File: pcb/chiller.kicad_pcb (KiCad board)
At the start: 2 copper layers, 94 x 57 mm, 68 parts, among them J1 Temp sensor 1, J10 Fan, J11 Display, J12 Debug, J13 Conn_01x04, J14 Flow sensor, J15 Buzzer, J2 Temp sensor 2, J3 Ext, J4 Mains in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

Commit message: Fix footprint.
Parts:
- D8: footprint Diode_SMD:D_SMC -> Diode_SMD:D_SMA
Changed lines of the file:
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@@
     )
   )
-  (footprint "Diode_SMD:D_SMC" (layer "F.Cu")
+  (footprint "Diode_SMD:D_SMA" (layer "F.Cu")
     (at 101.4984 128.524)
-    (descr "Diode SMC (DO-214AB)")
-    (tags "Diode SMC (DO-214AB)")
-    (property "Reference" "D8" (at -1.6764 -4.9784 0) (layer "F.SilkS") hide
+    (descr "Diode SMA (DO-214AC)")
+    (tags "Diode SMA (DO-214AC)")
+    (property "Reference" "D8" (at 0 -2.5 0) (layer "F.SilkS")
       (effects (font (size 1 1) (thickness 0.15)))
     )
-    (property "Value" "SS34" (at 0 4.2 0) (layer "F.Fab") hide
+    (property "Value" "SS34" (at 0 2.6 0) (layer "F.Fab")
       (effects (font (size 1 1) (thickness 0.15)))
     )
@@
     (sheetfile "chiller.kicad_sch")
     (attr smd)
-    (fp_line (start -4.8 -3.25) (end 3.6 -3.25)
+    (fp_line (start -3.4 -1.65) (end -3.4 1.65)
       (stroke (width 0.12) (type solid)) (layer "F.SilkS"))
-    (fp_line (start -4.8 3.25) (end -4.8 -3.25)
+    (fp_line (start -3.4 -1.65) (end 2 -1.65)
       (stroke (width 0.12) (type solid)) (layer "F.SilkS"))
-    (fp_line (start -4.8 3.25) (end 3.6 3.25)
+    (fp_line (start -3.4 1.65) (end 2 1.65)
       (stroke (width 0.12) (type solid)) (layer "F.SilkS"))
-    (fp_line (start -4.9 -3.35) (end 4.9 -3.35)
+    (fp_line (start -3.5 -1.75) (end 3.5 -1.75)
       (stroke (width 0.05) (type solid)) (layer "F.CrtYd"))
-    (fp_line (start -4.9 3.35) (end -4.9 -3.35)
+    (fp_line (start -3.5 1.75) (end -3.5 -1.75)
       (stroke (width 0.05) (type solid)) (layer "F.CrtYd"))
-    (fp_line (start 4.9 -3.35) (end 4.9 3.35)
+    (fp_line (start 3.5 -1.75) (end 3.5 1.75)
       (stroke (width 0.05) (type solid)) (layer "F.CrtYd"))
-    (fp_line (start 4.9 3.35) (end -4.9 3.35)
+    (fp_line (start 3.5 1.75) (end -3.5 1.75)
       (stroke (width 0.05) (type solid)) (layer "F.CrtYd"))
-    (fp_line (start -3.55 3.1) (end -3.55 -3.1)
+    (fp_line (start -2.3 1.5) (end -2.3 -1.5)
       (stroke (width 0.1) (type solid)) (layer "F.Fab"))
     (fp_line (start -0.64944 -0.79908) (end -0.64944 0.80112)
@@
     (fp_line (start 0.50118 0.75032) (end 0.50118 -0.79908)
       (stroke (width 0.1) (type solid)) (layer "F.Fab"))
-    (fp_line (start 3.55 -3.1) (end -3.55 -3.1)
+    (fp_line (start 2.3 -1.5) (end -2.3 -1.5)
       (stroke (width 0.1) (type solid)) (layer "F.Fab"))
-    (fp_line (start 3.55 -3.1) (end 3.55 3.1)
+    (fp_line (start 2.3 -1.5) (end 2.3 1.5)
       (stroke (width 0.1) (type solid)) (layer "F.Fab"))
-    (fp_line (start 3.55 3.1) (end -3.55 3.1)
+    (fp_line (start 2.3 1.5) (end -2.3 1.5)
       (stroke (width 0.1) (type solid)) (layer "F.Fab"))
-    (fp_text user "${REFERENCE}" (at 0 -1.9 0) (layer "F.Fab")
+    (fp_text user "${REFERENCE}" (at 0 -2.5 0) (layer "F.Fab")
       (effects (font (size 1 1) (thickness 0.15)))
     )
-    (pad "1" smd rect (at -3.4 0 90) (size 3.3 2.5) (layers "F.Cu" "F.Paste" "F.Mask")
+    (pad "1" smd rect (at -2 0) (size 2.5 1.8) (layers "F.Cu" "F.Paste" "F.Mask")
       (net 53 "+12V") (pinfunction "K") (pintype "passive")
     )
-    (pad "2" smd rect (at 3.4 0 90) (size 3.3 2.5) (layers "F.Cu" "F.Paste" "F.Mask")
+    (pad "2" smd rect (at 2 0) (size 2.5 1.8) (layers "F.Cu" "F.Paste" "F.Mask")
       (net 57 "Net-(D8-A)") (pinfunction "A") (pintype "passive")
     )
-    (model "${KICAD6_3DMODEL_DIR}/Diode_SMD.3dshapes/D_SMC.wrl"
+    (model "${KICAD6_3DMODEL_DIR}/Diode_SMD.3dshapes/D_SMA.wrl"
       (offset (xyz 0 0 0))
       (scale (xyz 1 1 1))
@@
   (segment (start 119.6593 125.6029) (end 119.6595 125.6029) (width 0.2) (layer "F.Cu") (net 53))
   (segment (start 120.724374 126.4542) (end 119.949374 125.6792) (width 0.2) (layer "F.Cu") (net 53))
+  (segment (start 99.4984 128.524) (end 104.5276 123.4948) (width 1) (layer "F.Cu") (net 53))
   (segment (start 136.1332 127.9652) (end 132.1044 127.9652) (width 0.2) (layer "F.Cu") (net 53))
-  (segment (start 96.980547 129.9972) (end 91.7448 129.9972) (width 1) (layer "F.Cu") (net 53))
   (segment (start 120.142 121.0964) (end 118.3894 119.3438) (width 0.2) (layer "F.Cu") (net 53))
-  (segment (start 98.0984 128.524) (end 98.0984 128.879347) (width 1) (layer "F.Cu") (net 53))
   (segment (start 90.5456 128.798) (end 90.5456 127.999) (width 1) (layer "F.Cu") (net 53))
+  (segment (start 98.0252 129.9972) (end 99.4984 128.524) (width 1) (layer "F.Cu") (net 53))
   (segment (start 109.8658 119.3184) (end 105.6894 123.4948) (width 1) (layer "F.Cu") (net 53))
   (segment (start 111.2266 119.3184) (end 109.8658 119.3184) (width 1) (layer "F.Cu") (net 53))
   (segment (start 120.142 125.1204) (end 120.142 121.0964) (width 0.2) (layer "F.Cu") (net 53))
-  (segment (start 98.0984 128.879347) (end 96.980547 129.9972) (width 1) (layer "F.Cu") (net 53))
   (segment (start 132.1044 127.9652) (end 131.3688 127.2296) (width 0.2) (layer "F.Cu") (net 53))
   (segment (start 119.583 125.6792) (end 119.688153 125.574047) (width 0.2) (layer "F.Cu") (net 53))
   (segment (start 119.949374 125.6792) (end 119.583 125.6792) (width 0.2) (layer "F.Cu") (net 53))
-  (segment (start 103.1276 123.4948) (end 98.0984 128.524) (width 1) (layer "F.Cu") (net 53))
   (segment (start 131.3688 127.2296) (end 130.684 127.2296) (width 0.2) (layer "F.Cu") (net 53))
   (segment (start 91.7448 129.9972) (end 90.5456 128.798) (width 1) (layer "F.Cu") (net 53))
   (segment (start 121.5266 126.4542) (end 120.724374 126.4542) (width 0.2) (layer "F.Cu") (net 53))
   (segment (start 130.098 126.6436) (end 121.716 126.6436) (width 0.2) (layer "F.Cu") (net 53))
+  (segment (start 104.5276 123.4948) (end 105.6894 123.4948) (width 1) (layer "F.Cu") (net 53))
   (segment (start 111.2266 119.3184) (end 118.364 119.3184) (width 1) (layer "F.Cu") (net 53))
   (segment (start 121.716 126.6436) (end 121.5266 126.4542) (width 0.2) (layer "F.Cu") (net 53))
+  (segment (start 91.7448 129.9972) (end 98.0252 129.9972) (width 1) (layer "F.Cu") (net 53))
   (segment (start 119.6595 125.6029) (end 120.142 125.1204) (width 0.2) (layer "F.Cu") (net 53))
   (segment (start 130.684 127.2296) (end 130.098 126.6436) (width 0.2) (layer "F.Cu") (net 53))
-  (segment (start 105.6894 123.4948) (end 103.1276 123.4948) (width 1) (layer "F.Cu") (net 53))
   (segment (start 119.583 125.6792) (end 119.6593 125.6029) (width 0.2) (layer "F.Cu") (net 53))
   (segment (start 95.631 116.7383) (end 94.0816 116.7383) (width 0.2) (layer "F.Cu") (net 54))
@@
   (segment (start 119.9388 106.575949) (end 125.529251 112.1664) (width 0.2) (layer "B.Cu") (net 56))
   (segment (start 127.508 125.7808) (end 124.0791 129.2097) (width 0.2) (layer "B.Cu") (net 56))
-  (segment (start 88.7984 126.7968) (end 88.7984 129.286) (width 1) (layer "F.Cu") (net 57))
-  (segment (start 104.8984 128.524) (end 110.6498 128.524) (width 1) (layer "F.Cu") (net 57))
-  (segment (start 93.0456 127.999) (end 93.0456 127.002742) (width 1) (layer "F.Cu") (net 57))
+  (segment (start 103.4984 128.524) (end 110.6498 128.524) (width 1) (layer "F.Cu") (net 57))
+  (segment (start 93.0456 127.002742) (end 91.925258 125.8824) (width 1) (layer "F.Cu") (net 57))
+  (segment (start 88.7984 129.286) (end 90.733096 131.220696) (width 1) (layer "F.Cu") (net 57))
   (segment (start 91.925258 125.8824) (end 89.7128 125.8824) (width 1) (layer "F.Cu") (net 57))
   (segment (start 110.7444 128.7272) (end 110.7454 128.7282) (width 1) (layer "F.Cu") (net 57))
-  (segment (start 102.4636 131.2164) (end 104.8984 128.524) (width 1) (layer "F.Cu") (net 57))
-  (segment (start 88.7984 129.286) (end 90.733096 131.220696) (width 1) (layer "F.Cu") (net 57))
   (segment (start 89.7128 125.8824) (end 88.7984 126.7968) (width 1) (layer "F.Cu") (net 57))
+  (segment (start 90.733096 131.220696) (end 100.801704 131.220696) (width 1) (layer "F.Cu") (net 57))
+  (segment (start 93.0456 127.999) (end 93.0456 127.002742) (width 1) (layer "F.Cu") (net 57))
+  (segment (start 88.7984 126.7968) (end 88.7984 129.286) (width 1) (layer "F.Cu") (net 57))
+  (segment (start 100.801704 131.220696) (end 103.4984 128.524) (width 1) (layer "F.Cu") (net 57))
   (segment (start 110.6498 128.524) (end 110.7454 128.4284) (width 1) (layer "F.Cu") (net 57))
-  (segment (start 90.733096 131.220696) (end 102.4636 131.2164) (width 1) (layer "F.Cu") (net 57))
-  (segment (start 93.0456 127.002742) (end 91.925258 125.8824) (width 1) (layer "F.Cu") (net 57))
   (segment (start 95.25 96.012) (end 95.25 94.8436) (width 0.2) (layer "F.Cu") (net 58))
   (segment (start 114.6897 102.8552) (end 109.992122 98.157622) (width 0.2) (layer "F.Cu") (net 58))

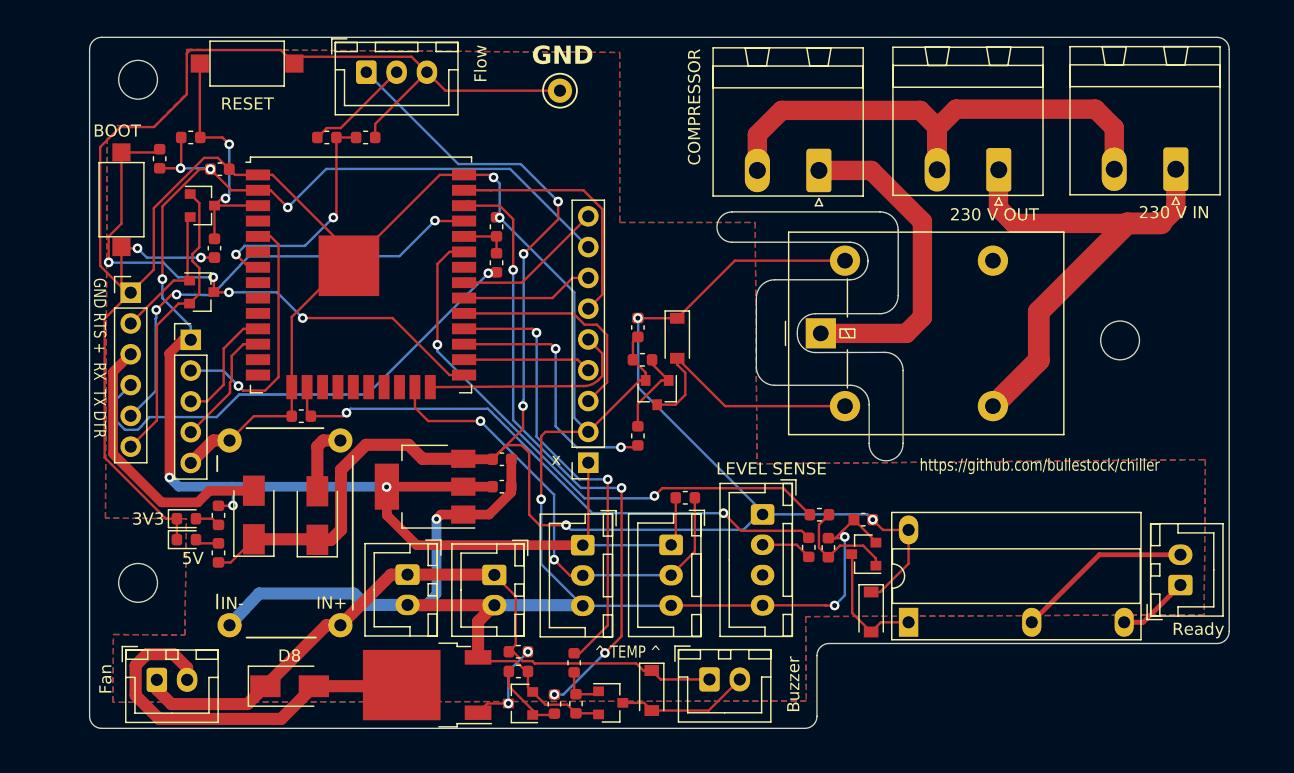
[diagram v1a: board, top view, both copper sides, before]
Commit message: Add inverters, stitching vias.
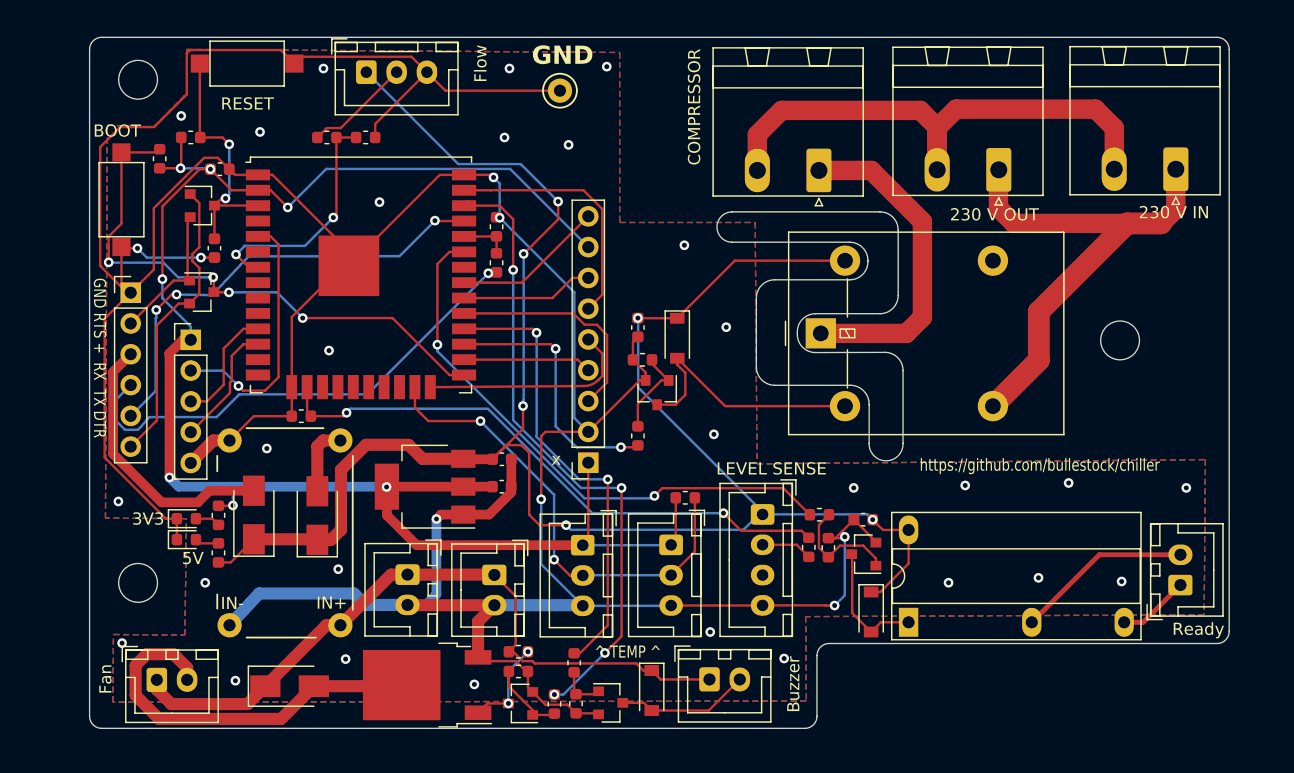
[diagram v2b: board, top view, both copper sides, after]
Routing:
- net GND: vias 8 -> 37

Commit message: Add new components.
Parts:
- removed Q5: BSS138, Package_TO_SOT_SMD:SOT-23
- removed R20: 1k, Resistor_SMD:R_0603_1608Metric
- added C7: 100n, Capacitor_SMD_AKL:C_0603_1608Metric, F.Cu at (122.8, 83.4)
- added D9: LED, LED_SMD:LED_0603_1608Metric, F.Cu at (126.0, 81.9)
- added U4: 74LVC2G14, Package_TO_SOT_SMD:SOT-23-6, F.Cu at (118.9, 82.3)
- C1, C2, C3, C4, C5: footprint Capacitor_SMD:C_0603_1608Metric -> Capacitor_SMD_AKL:C_0603_1608Metric
- C6: value 100n -> 1u; footprint Capacitor_SMD:C_0603_1608Metric -> Capacitor_SMD_AKL:C_0603_1608Metric
- R1, R10, R11, R12, R13, R14, R15, R17, R19, R2, R3, R4, R5, R6, R7, R8, R9: footprint Resistor_SMD:R_0603_1608Metric -> Resistor_SMD_AKL:R_0603_1608Metric
- R16: value 10k -> R_0603; footprint Resistor_SMD:R_0603_1608Metric -> Resistor_SMD_AKL:R_0603_1608Metric
- R18: value 10k -> 1k; footprint Resistor_SMD:R_0603_1608Metric -> Resistor_SMD_AKL:R_0603_1608Metric
- moved R16 42.0 mm to (125.3, 85.6)
- moved R18 4.71 mm to (125.0, 126.7), turned to -90 degrees
- moved R15 3.66 mm to (119.7, 129.9)
- moved R2 0.23 mm to (118.6, 93.8)
- moved R12 0.17 mm to (95.6, 117.7)
- moved R4 0.16 mm to (146.1, 117.1)
- moved R19 0.10 mm to (125.2, 130.0)
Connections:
- Q6 pad 1: Net-(Q5-D) -> Net-(Q6-G)
- R10 pad 1: Flow -> Net-(R10-Pad1)
- R11 pad 1: Flow -> Net-(R10-Pad1)
- R15 pad 1: Fan -> Net-(R15-Pad1)
- R15 pad 2: Net-(Q5-G) -> Net-(Q6-G)
- R16 pad 1: Net-(Q5-G) -> Flow
- R16 pad 2: GND -> Net-(D9-A)
- R18 pad 1: +12V -> Buzzer
- R18 pad 2: Net-(Q5-D) -> Net-(Q7-G)
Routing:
- net Fan: track 52.7 -> 0.55 mm, vias 4 -> 0
- net Flow: track 19.9 -> 0.76 mm, vias 2 -> 0
- net GND: track 328.3 -> 316.9 mm, vias 37 -> 35
- net Net-(Q5-D): track 7.75 -> 0.00 mm, vias 2 -> 0
- net Net-(Q5-G): track 6.25 -> 0.00 mm
- net Net-(Q6-G): track 0.00 -> 2.65 mm
- net +12V: track 58.5 -> 57.2 mm

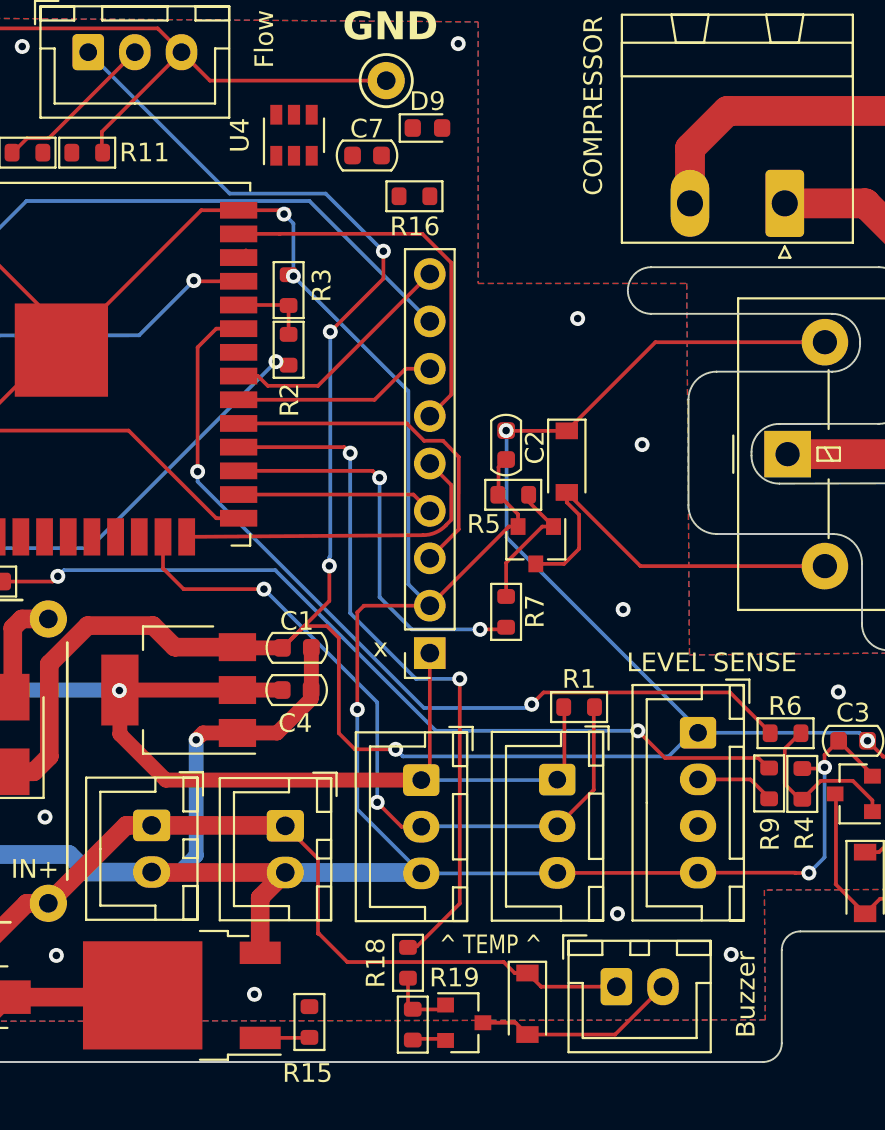
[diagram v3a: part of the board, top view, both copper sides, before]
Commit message: Add MOSFET to control OneWire power.
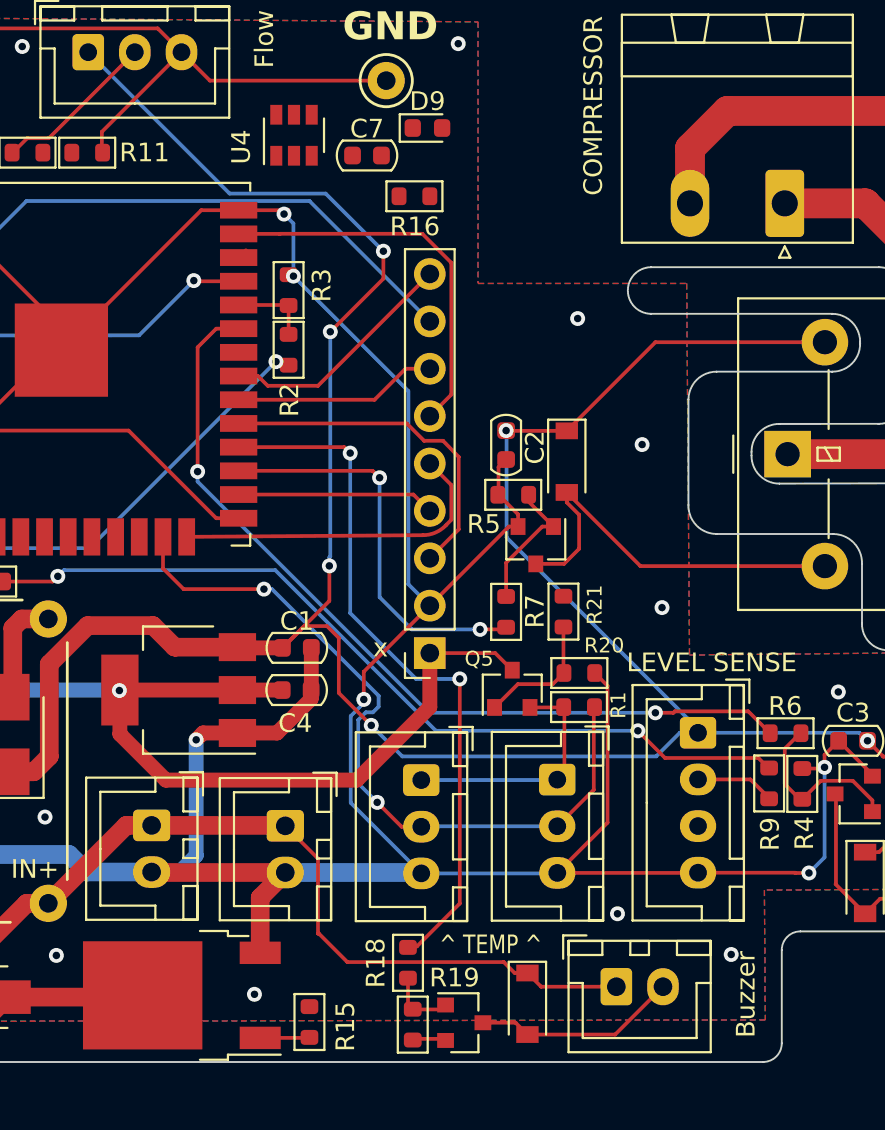
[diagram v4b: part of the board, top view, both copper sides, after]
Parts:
- added Q5: BSS138, Package_TO_SOT_SMD:SOT-23, F.Cu at (130.6, 112.0)
- added R20: 10k, Resistor_SMD_AKL:R_0603_1608Metric, F.Cu at (134.2, 111.2)
- added R21: 1k, Resistor_SMD_AKL:R_0603_1608Metric, F.Cu at (133.3, 107.9)
- R16: value R_0603 -> 1k
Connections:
- J1 pad 1: +3V3 -> Net-(J1-Pin_1)
- J2 pad 1: +3V3 -> Net-(J1-Pin_1)
- R1 pad 1: +3V3 -> Net-(J1-Pin_1)
- U1 pad 10: unconnected-(U1-IO25-Pad10) -> OW_PWR
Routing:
- net Net-(J1-Pin_1): track 0.00 -> 13.8 mm
- net GND: track 316.9 -> 327.2 mm
- net +3V3: track 140.5 -> 131.9 mm
- net Net-(Q5-G): track 0.00 -> 6.96 mm
- net TempSensor: track 38.9 -> 40.3 mm
- net +5V: track 162.0 -> 160.7 mm
- net Relay_ready: track 46.8 -> 46.2 mm
